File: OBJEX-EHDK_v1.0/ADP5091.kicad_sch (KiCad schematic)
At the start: 14 parts

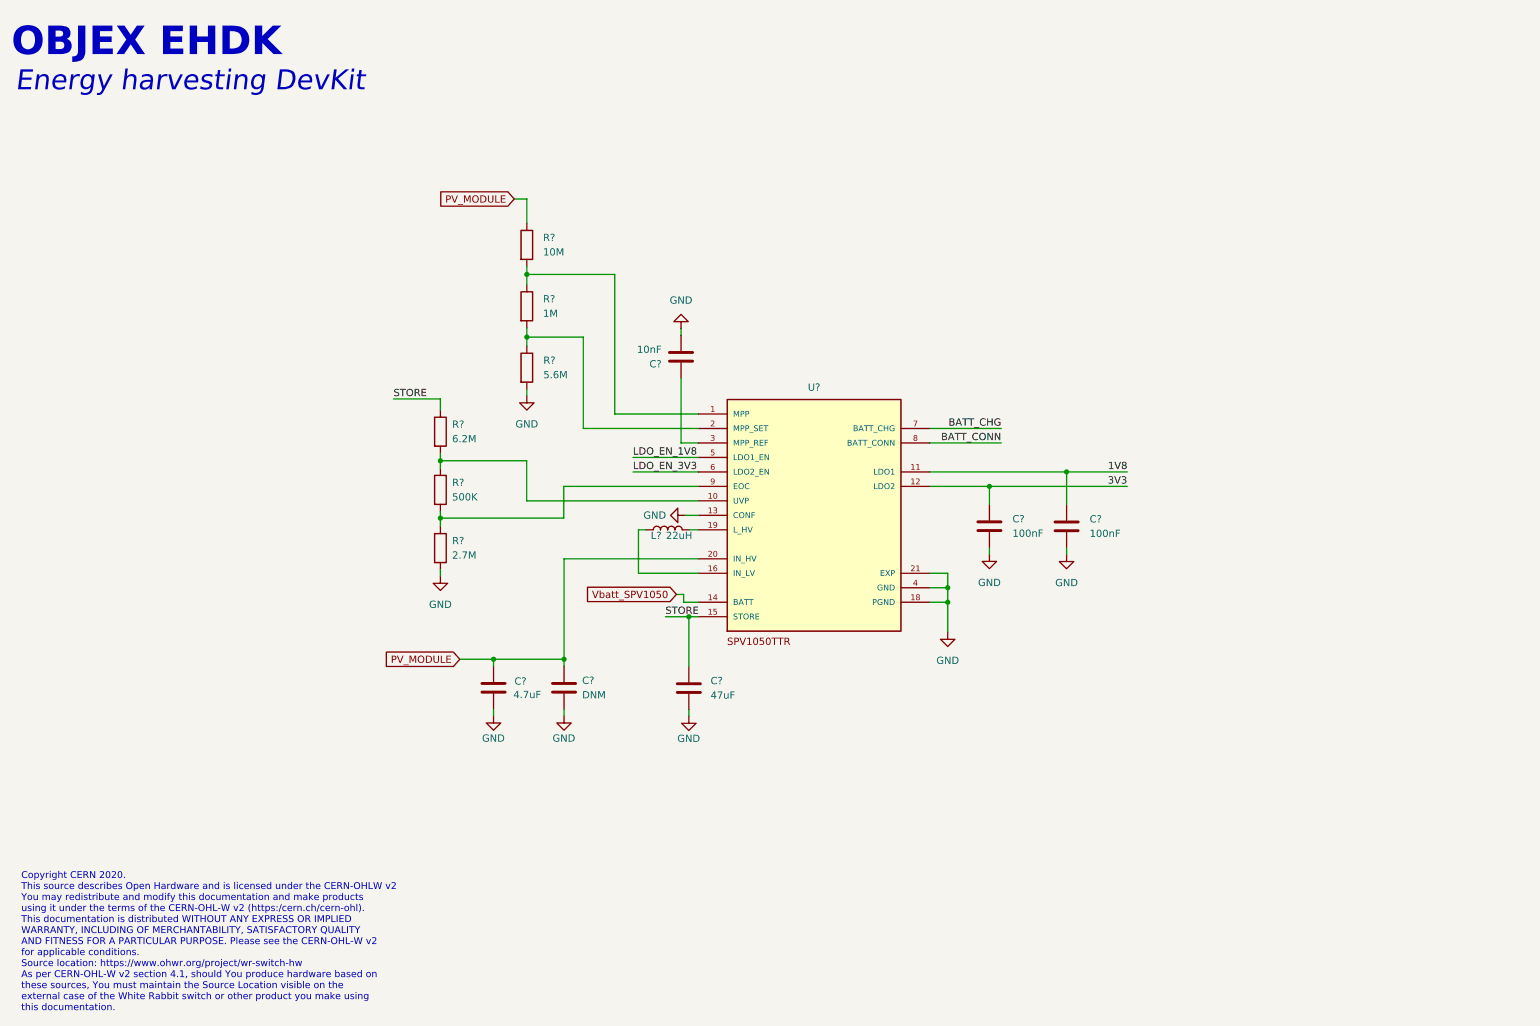
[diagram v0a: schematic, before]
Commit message: add: ADP5091
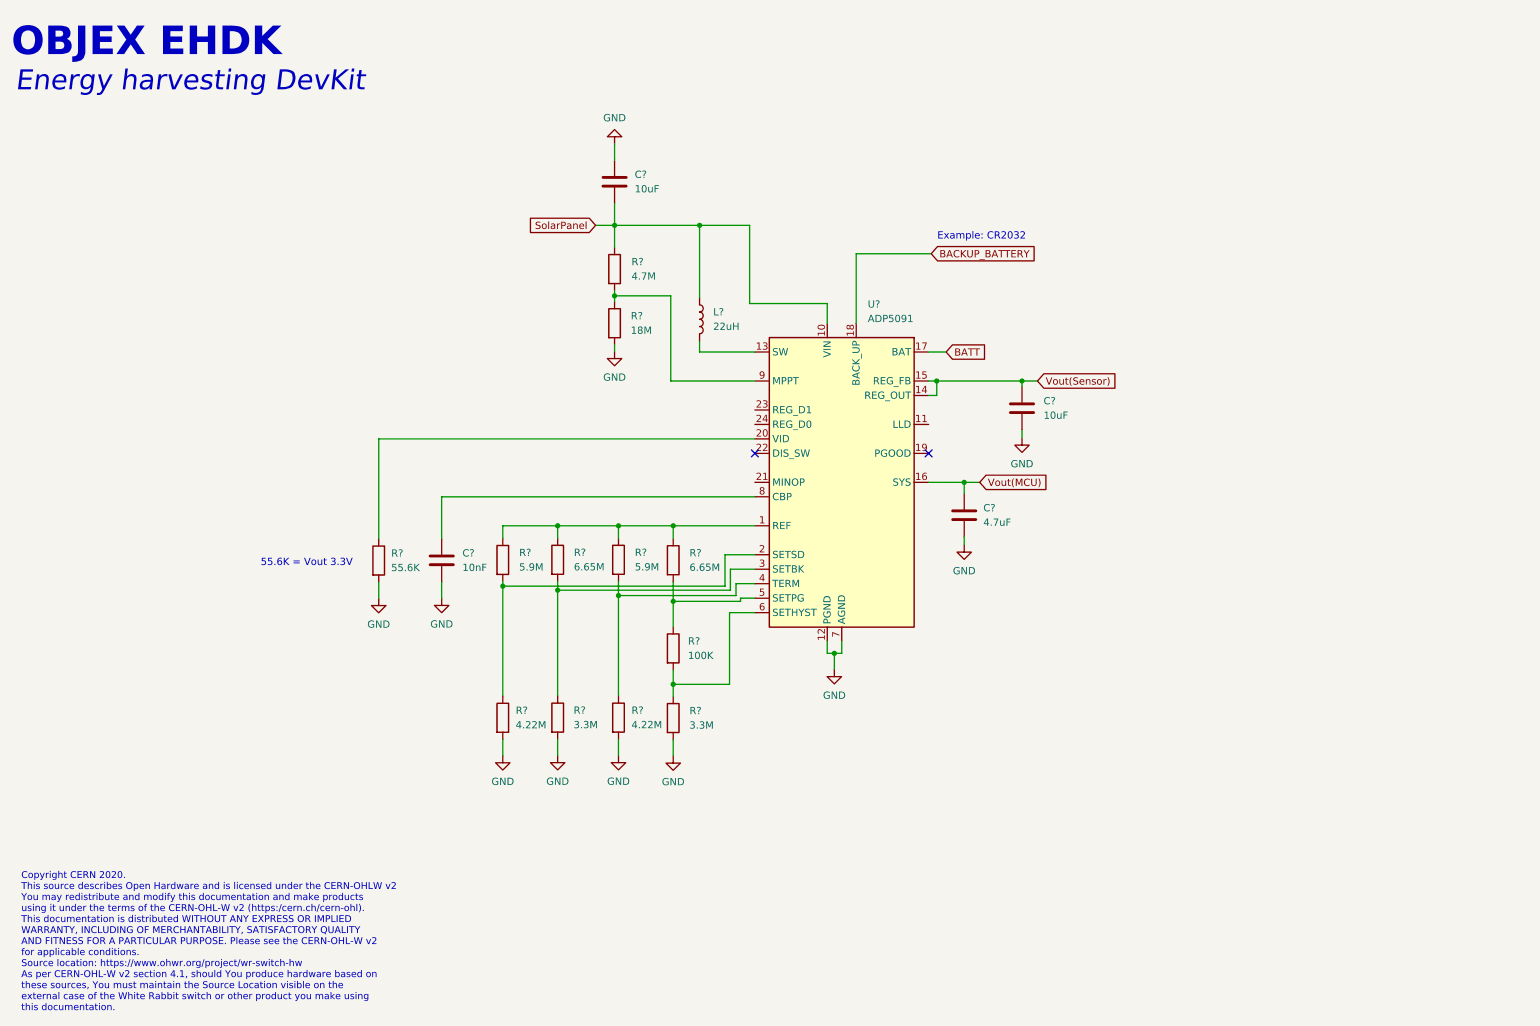
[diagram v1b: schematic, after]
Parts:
- removed C?: 10nF, symbol Device:C
- removed C?: 4.7uF, symbol Device:C
- removed C? (x2): 100nF, symbol Device:C
- removed C?: DNM, symbol Device:C
- removed C?: 47uF, symbol Device:C
- removed L?: 22uH, symbol Device:L
- removed R?: 6.2M, symbol Device:R
- removed R?: 2.7M, symbol Device:R
- removed R?: 5.6M, symbol Device:R
- removed R?: 10M, symbol Device:R
- removed R?: 1M, symbol Device:R
- removed R?: 500K, symbol Device:R
- removed U?: SPV1050TTR, QFN40P300X300X100-21N, symbol SPV1050TTR:SPV1050TTR
- added C?: 4.7uF, symbol Device:C
- added C?: 10nF, symbol Device:C
- added C? (x2): 10uF, symbol Device:C
- added L?: 22uH, symbol Device:L
- added R? (x2): 3.3M, symbol Device:R
- added R? (x2): 4.22M, symbol Device:R
- added R? (x2): 5.9M, symbol Device:R
- added R? (x2): 6.65M, symbol Device:R
- added R?: 100K, symbol Device:R
- added R?: 4.7M, symbol Device:R
- added R?: 18M, symbol Device:R
- added R?: 55.6K, symbol Device:R
- added U?: ADP5091, Package_CSP:LFCSP-24-1EP_4x4mm_P0.5mm_EP2.3x2.3mm, symbol Battery_Management:ADP5091
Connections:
- net GND: now also C?.1, C?.2, C?.2, C?.2, R?.2, R?.2, R?.2, R?.2, R?.2, R?.2, U?.12 (PGND), U?.25 (AGND), U?.7 (AGND)
- new net: R?.1, R?.2, U?.3 (SETBK)
- new net: R?.1, R?.2, U?.6 (SETHYST)
- new net: R?.1, R?.2, U?.2 (SETSD)
- new net: R?.1, R?.1, R?.1, R?.1, U?.1 (REF)
- new net: R?.1, R?.2, U?.4 (TERM)
- new net: L?.2, U?.13 (SW)
- new net: R?.1, U?.20 (VID)
- new net: R?.1, R?.2, U?.5 (SETPG)
- new net: C?.1, U?.8 (CBP)
- new net: R?.1, R?.2, U?.9 (MPPT)
- new net BACKUP_BATTERY: U?.18 (BACK_UP)
- new net BATT: U?.17 (BAT)
- new net SolarPanel: C?.2, L?.1, R?.1, U?.10 (VIN)
- new net Vout(MCU): C?.1, U?.16 (SYS)
- new net Vout(Sensor): C?.1, U?.14 (REG_OUT), U?.15 (REG_FB)
- no-connect marks 0 -> 2
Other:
- note added: "55.6K = Vout 3.3V"
- note added: "Example: CR2032"

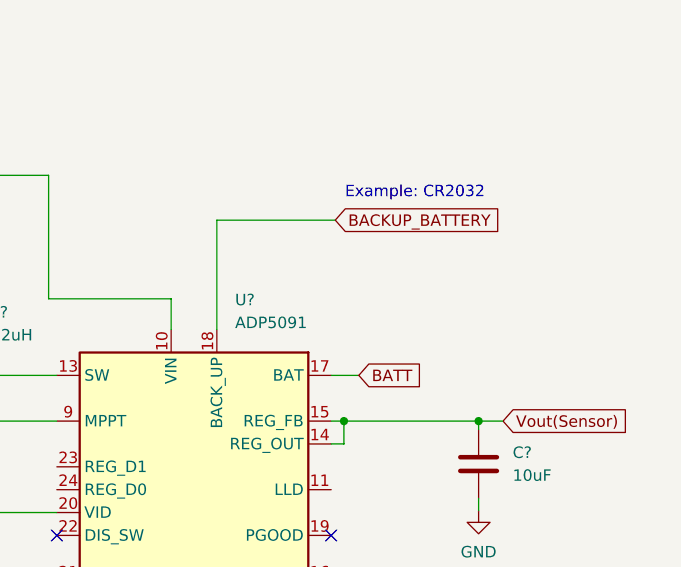
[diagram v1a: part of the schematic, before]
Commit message: Update design, EH ICs & Battery conn
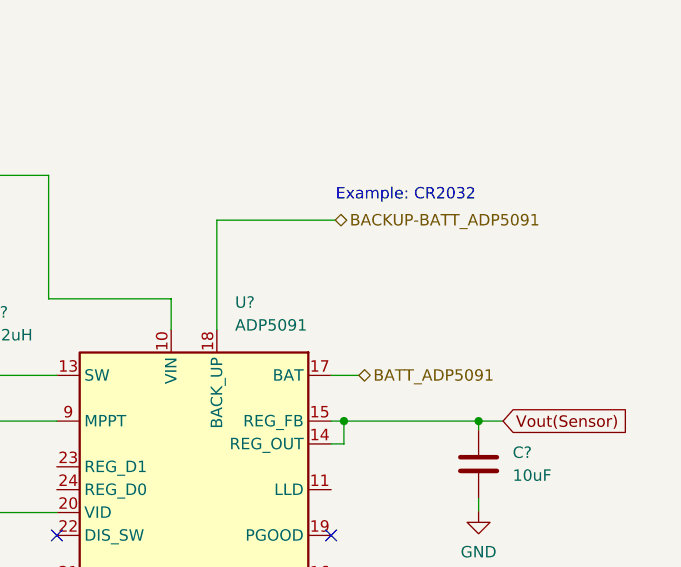
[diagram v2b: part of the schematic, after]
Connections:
- net BACKUP_BATTERY renamed BACKUP-BATT_ADP5091
- net BATT renamed BATT_ADP5091
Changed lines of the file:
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@@
     (effects (font (size 1.27 1.27)) (justify left bottom))
   )
-  (text "Example: CR2032\n" (at 179.3494 58.4454 0)
+  (text "Example: CR2032\n" (at 178.3334 58.6994 0)
     (effects (font (size 1.27 1.27)) (justify left bottom))
   )
   (text "Energy harvesting DevKit" (at 17.6022 32.5374 0)
     (effects (font (size 3.5 3.5) italic) (justify left bottom))
-  )
-  (global_label "BACKUP_BATTERY" (shape input) (at 178.2826 60.706 0) (fields_autoplaced)
-    (effects (font (size 1.27 1.27)) (justify left))
-    (property "Intersheet References" "${INTERSHEET_REFS}" (id 0) (at 196.9638 60.6266 0)
-      (effects (font (size 1.27 1.27)) (justify left) hide)
-    )
   )
   (global_label "Vout(MCU)" (shape input) (at 186.7916 100.8126 0) (fields_autoplaced)
@@
     )
   )
-  (global_label "BATT" (shape input) (at 180.8988 77.9526 0) (fields_autoplaced)
+  (hierarchical_label "BACKUP-BATT_ADP5091" (shape bidirectional) (at 178.2826 60.706 0)
     (effects (font (size 1.27 1.27)) (justify left))
-    (property "Intersheet References" "${INTERSHEET_REFS}" (id 0) (at 187.6057 77.8732 0)
-      (effects (font (size 1.27 1.27)) (justify left) hide)
-    )
+  )
+  (hierarchical_label "BATT_ADP5091" (shape bidirectional) (at 180.8988 77.9526 0)
+    (effects (font (size 1.27 1.27)) (justify left))
   )
   (symbol (lib_id "Device:R") (at 112.7506 142.0876 0) (unit 1)
@@
   (symbol (lib_id "Battery_Management:ADP5091") (at 162.5854 100.8126 0) (unit 1)
     (in_bom yes) (on_board yes) (fields_autoplaced)
-    (property "Reference" "U?" (id 0) (at 167.1448 69.5706 0)
+    (property "Reference" "U?" (id 0) (at 167.1448 69.85 0)
       (effects (font (size 1.27 1.27)) (justify left))
     )
-    (property "Value" "ADP5091" (id 1) (at 167.1448 72.1106 0)
+    (property "Value" "ADP5091" (id 1) (at 167.1448 72.39 0)
       (effects (font (size 1.27 1.27)) (justify left))
     )

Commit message: fix some things
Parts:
- added J?: Vout1, symbol Connector_Generic:Conn_01x02
- added J?: Solar, symbol Connector_Generic:Conn_01x02
- added J?: Conn_01x03, symbol Connector_Generic:Conn_01x03
- added J?: Vout2, symbol Connector_Generic:Conn_01x02
- added JP?: SolderJumper_3_Open, symbol Jumper:SolderJumper_3_Open
- added R?: 150K, symbol Device:R
- added R?: 14K, symbol Device:R
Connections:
- net GND: now also J?.1 (Pin_1), J?.2 (Pin_2), J?.2 (Pin_2), R?.2, R?.2
- net SolarPanel: now also J?.2 (Pin_2)
- net Vout(MCU): now also J?.1 (Pin_1)
- net LLD: now reaches U?.11 (LLD)
- net LLD: now also J?.1 (Pin_1)
- net at U?.20 (VID): now also JP?.3 (B); no longer R?.1
- net at U?.21 (MINOP): now also R?.1
- net REG_D1: now reaches U?.23 (REG_D1)
- net REG_D1: now also J?.2 (Pin_2)
- net REG_D0: now reaches U?.24 (REG_D0)
- net REG_D0: now also J?.3 (Pin_3)
- net Vout(Sensor) renamed Vout(Sens)
- net Vout(Sens): now also J?.1 (Pin_1)
- new net: JP?.2 (C), R?.1
- new net: JP?.1 (A), R?.1
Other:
- note added: "14K = Vout 1.8V"
- moved on the sheet: C?, R?

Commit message: update sch
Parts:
- removed J?: Conn_01x03, symbol Connector_Generic:Conn_01x03
- added J?: Conn_01x02, symbol Connector_Generic:Conn_01x02
- added J?: TestPoint - Black, symbol Connector_Generic:Conn_01x01
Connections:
- net LLD: now also J?.1 (Pin_1)
- net REG_D0: now also J?.2 (Pin_2)
- net REG_D1: now also J?.1 (Pin_1)
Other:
- note added: "Dim foro min 1mm"
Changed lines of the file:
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@@
     (stroke (width 0) (type default) (color 0 0 0 0))
   )
-  (wire (pts (xy 223.4692 129.667) (xy 231.1908 129.667))
+  (wire (pts (xy 199.6694 139.8778) (xy 207.391 139.8778))
     (stroke (width 0) (type default) (color 0 0 0 0))
   )
@@
     (stroke (width 0) (type default) (color 0 0 0 0))
   )
-  (wire (pts (xy 223.4692 127.127) (xy 231.1908 127.127))
+  (wire (pts (xy 199.6694 137.3378) (xy 207.391 137.3378))
     (stroke (width 0) (type default) (color 0 0 0 0))
   )
@@
     (stroke (width 0) (type default) (color 0 0 0 0))
   )
-  (wire (pts (xy 223.4692 124.587) (xy 231.1908 124.587))
+  (wire (pts (xy 243.6622 136.7028) (xy 251.3838 136.7028))
     (stroke (width 0) (type default) (color 0 0 0 0))
   )
@@
     (effects (font (size 1.27 1.27)) (justify left bottom))
   )
-  (label "REG_D1" (at 223.4692 127.127 0)
+  (text "Dim foro min 1mm" (at 254.7874 142.0368 0)
+    (effects (font (size 1.27 1.27)) (justify left bottom))
+  )
+  (label "REG_D1" (at 199.6694 137.3378 0)
     (effects (font (size 1.27 1.27)) (justify left bottom))
   )
@@
     (effects (font (size 1.27 1.27)) (justify left bottom))
   )
-  (label "LLD" (at 223.4692 124.587 0)
+  (label "LLD" (at 243.6622 136.7028 0)
     (effects (font (size 1.27 1.27)) (justify left bottom))
   )
@@
     (effects (font (size 1.27 1.27)) (justify right bottom))
   )
-  (label "REG_D0" (at 223.4692 129.667 0)
+  (label "REG_D0" (at 199.6694 139.8778 0)
     (effects (font (size 1.27 1.27)) (justify left bottom))
   )
@@
     (pin "1")
   )
+  (symbol (lib_id "Connector_Generic:Conn_01x02") (at 212.471 137.3378 0) (unit 1)
+    (in_bom yes) (on_board yes) (fields_autoplaced)
+    (property "Reference" "J?" (id 0) (at 215.4936 137.3377 0)
+      (effects (font (size 1.27 1.27)) (justify left))
+    )
+    (property "Value" "Conn_01x02" (id 1) (at 215.4936 139.8777 0)
+      (effects (font (size 1.27 1.27)) (justify left))
+    )
+    (property "Footprint" "" (id 2) (at 212.471 137.3378 0)
+      (effects (font (size 1.27 1.27)) hide)
+    )
+    (property "Datasheet" "~" (id 3) (at 212.471 137.3378 0)
+      (effects (font (size 1.27 1.27)) hide)
+    )
+    (pin "1")
+    (pin "2")
+  )
   (symbol (lib_id "Device:R") (at 112.7506 114.4016 0) (unit 1)
     (in_bom yes) (on_board yes) (fields_autoplaced)
@@
     (pin "1")
     (pin "2")
-  )
-  (symbol (lib_id "Connector_Generic:Conn_01x03") (at 236.2708 127.127 0) (unit 1)
-    (in_bom yes) (on_board yes) (fields_autoplaced)
-    (property "Reference" "J?" (id 0) (at 239.268 125.8569 0)
-      (effects (font (size 1.27 1.27)) (justify left))
-    )
-    (property "Value" "Conn_01x03" (id 1) (at 239.268 128.3969 0)
-      (effects (font (size 1.27 1.27)) (justify left))
-    )
-    (property "Footprint" "" (id 2) (at 236.2708 127.127 0)
-      (effects (font (size 1.27 1.27)) hide)
-    )
-    (property "Datasheet" "~" (id 3) (at 236.2708 127.127 0)
-      (effects (font (size 1.27 1.27)) hide)
-    )
-    (pin "1")
-    (pin "2")
-    (pin "3")
   )
   (symbol (lib_id "power:GND") (at 103.124 148.7424 0) (unit 1)
@@
     (pin "3")
   )
+  (symbol (lib_id "Connector_Generic:Conn_01x01") (at 256.4638 136.7028 0) (unit 1)
+    (in_bom yes) (on_board yes) (fields_autoplaced)
+    (property "Reference" "J?" (id 0) (at 259.1054 135.4327 0)
+      (effects (font (size 1.27 1.27)) (justify left))
+    )
+    (property "Value" "TestPoint - Black" (id 1) (at 259.1054 137.9727 0)
+      (effects (font (size 1.27 1.27)) (justify left))
+    )
+    (property "Footprint" "" (id 2) (at 256.4638 136.7028 0)
+      (effects (font (size 1.27 1.27)) hide)
+    )
+    (property "Datasheet" "~" (id 3) (at 256.4638 136.7028 0)
+      (effects (font (size 1.27 1.27)) hide)
+    )
+    (pin "1")
+  )
   (symbol (lib_id "Connector_Generic:Conn_01x02") (at 219.6084 83.0326 0) (unit 1)
